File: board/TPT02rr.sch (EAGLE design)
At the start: 16 parts, among them SW4 SW_SLIDECUS12B, U1 MOD_CYBLE014008-00, U2 REG_TPS61221

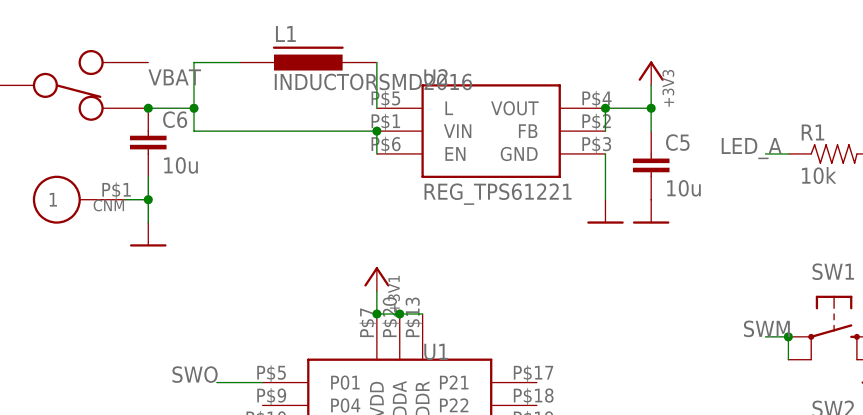
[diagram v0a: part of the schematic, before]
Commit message: Cの部品番号を整理。Elecrow向けBOMを作成。
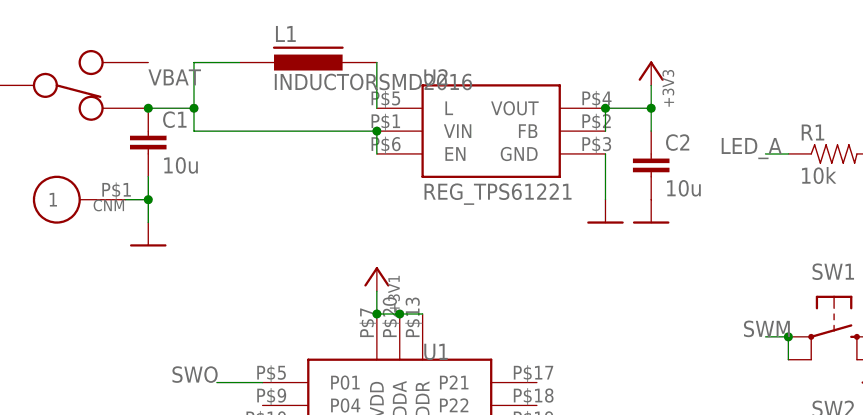
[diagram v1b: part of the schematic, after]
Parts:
- renumbered C5 to C2, C6 to C1
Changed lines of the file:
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@@
 <?xml version="1.0" encoding="utf-8"?>
 <!DOCTYPE eagle SYSTEM "eagle.dtd">
-<eagle version="7.5.0">
+<eagle version="7.7.0">
 <drawing>
 <settings>
@@
 <grid distance="0.1" unitdist="inch" unit="inch" style="lines" multiple="1" display="no" altdistance="0.01" altunitdist="inch" altunit="inch"/>
 <layers>
-<layer number="1" name="Top" color="4" fill="1" visible="yes" active="no"/>
-<layer number="16" name="Bottom" color="1" fill="1" visible="yes" active="no"/>
-<layer number="17" name="Pads" color="2" fill="1" visible="yes" active="no"/>
-<layer number="18" name="Vias" color="2" fill="1" visible="yes" active="no"/>
-<layer number="19" name="Unrouted" color="6" fill="1" visible="yes" active="no"/>
-<layer number="20" name="Dimension" color="15" fill="1" visible="yes" active="no"/>
-<layer number="21" name="tPlace" color="7" fill="1" visible="yes" active="no"/>
-<layer number="22" name="bPlace" color="7" fill="1" visible="yes" active="no"/>
-<layer number="23" name="tOrigins" color="15" fill="1" visible="yes" active="no"/>
-<layer number="24" name="bOrigins" color="15" fill="1" visible="yes" active="no"/>
-<layer number="25" name="tNames" color="7" fill="1" visible="yes" active="no"/>
-<layer number="26" name="bNames" color="7" fill="1" visible="yes" active="no"/>
-<layer number="27" name="tValues" color="7" fill="1" visible="yes" active="no"/>
-<layer number="28" name="bValues" color="7" fill="1" visible="yes" active="no"/>
+<layer number="1" name="Top" color="4" fill="1" visible="no" active="no"/>
+<layer number="16" name="Bottom" color="1" fill="1" visible="no" active="no"/>
+<layer number="17" name="Pads" color="2" fill="1" visible="no" active="no"/>
+<layer number="18" name="Vias" color="2" fill="1" visible="no" active="no"/>
+<layer number="19" name="Unrouted" color="6" fill="1" visible="no" active="no"/>
+<layer number="20" name="Dimension" color="15" fill="1" visible="no" active="no"/>
+<layer number="21" name="tPlace" color="7" fill="1" visible="no" active="no"/>
+<layer number="22" name="bPlace" color="7" fill="1" visible="no" active="no"/>
+<layer number="23" name="tOrigins" color="15" fill="1" visible="no" active="no"/>
+<layer number="24" name="bOrigins" color="15" fill="1" visible="no" active="no"/>
+<layer number="25" name="tNames" color="7" fill="1" visible="no" active="no"/>
+<layer number="26" name="bNames" color="7" fill="1" visible="no" active="no"/>
+<layer number="27" name="tValues" color="7" fill="1" visible="no" active="no"/>
+<layer number="28" name="bValues" color="7" fill="1" visible="no" active="no"/>
 <layer number="29" name="tStop" color="7" fill="3" visible="no" active="no"/>
 <layer number="30" name="bStop" color="7" fill="6" visible="no" active="no"/>
@@
 <layer number="35" name="tGlue" color="7" fill="4" visible="no" active="no"/>
 <layer number="36" name="bGlue" color="7" fill="5" visible="no" active="no"/>
-<layer number="37" name="tTest" color="7" fill="1" visible="yes" active="no"/>
-<layer number="38" name="bTest" color="7" fill="1" visible="yes" active="no"/>
+<layer number="37" name="tTest" color="7" fill="1" visible="no" active="no"/>
+<layer number="38" name="bTest" color="7" fill="1" visible="no" active="no"/>
 <layer number="39" name="tKeepout" color="4" fill="11" visible="no" active="no"/>
 <layer number="40" name="bKeepout" color="1" fill="11" visible="no" active="no"/>
@@
 <layer number="44" name="Drills" color="7" fill="1" visible="no" active="no"/>
 <layer number="45" name="Holes" color="7" fill="1" visible="no" active="no"/>
-<layer number="46" name="Milling" color="3" fill="1" visible="yes" active="no"/>
-<layer number="47" name="Measures" color="7" fill="1" visible="yes" active="no"/>
-<layer number="48" name="Document" color="7" fill="1" visible="yes" active="no"/>
-<layer number="49" name="Reference" color="7" fill="1" visible="yes" active="no"/>
-<layer number="50" name="dxf" color="7" fill="1" visible="yes" active="no"/>
-<layer number="51" name="tDocu" color="7" fill="1" visible="yes" active="no"/>
-<layer number="52" name="bDocu" color="7" fill="1" visible="yes" active="no"/>
-<layer number="53" name="tGND_GNDA" color="7" fill="9" visible="yes" active="no"/>
-<layer number="54" name="bGND_GNDA" color="1" fill="9" visible="yes" active="no"/>
-<layer number="56" name="wert" color="7" fill="1" visible="yes" active="no"/>
-<layer number="57" name="tCAD" color="7" fill="1" visible="yes" active="no"/>
-<layer number="59" name="Invisible" color="7" fill="1" visible="yes" active="no"/>
-<layer number="61" name="stand" color="7" fill="1" visible="yes" active="no"/>
+<layer number="46" name="Milling" color="3" fill="1" visible="no" active="no"/>
+<layer number="47" name="Measures" color="7" fill="1" visible="no" active="no"/>
+<layer number="48" name="Document" color="7" fill="1" visible="no" active="no"/>
+<layer number="49" name="Reference" color="7" fill="1" visible="no" active="no"/>
+<layer number="50" name="dxf" color="7" fill="1" visible="no" active="no"/>
+<layer number="51" name="tDocu" color="7" fill="1" visible="no" active="no"/>
+<layer number="52" name="bDocu" color="7" fill="1" visible="no" active="no"/>
+<layer number="53" name="tGND_GNDA" color="7" fill="9" visible="no" active="no"/>
+<layer number="54" name="bGND_GNDA" color="1" fill="9" visible="no" active="no"/>
+<layer number="56" name="wert" color="7" fill="1" visible="no" active="no"/>
+<layer number="57" name="tCAD" color="7" fill="1" visible="no" active="no"/>
+<layer number="59" name="Invisible" color="7" fill="1" visible="no" active="no"/>
+<layer number="61" name="stand" color="7" fill="1" visible="no" active="no"/>
 <layer number="90" name="Modules" color="5" fill="1" visible="yes" active="yes"/>
 <layer number="91" name="Nets" color="2" fill="1" visible="yes" active="yes"/>
@@
 <part name="+3V3" library="akita" deviceset="POW_+3V3" device=""/>
 <part name="GND3" library="akita" deviceset="POW_GND" device=""/>
-<part name="C5" library="akita" deviceset="CAP" device="0603" value="10u"/>
+<part name="C2" library="akita" deviceset="CAP" device="0603" value="10u"/>
 <part name="GND5" library="akita" deviceset="POW_GND" device=""/>
-<part name="C6" library="akita" deviceset="CAP" device="0603" value="10u"/>
+<part name="C1" library="akita" deviceset="CAP" device="0603" value="10u"/>
 <part name="GND6" library="akita" deviceset="POW_GND" device=""/>
 <part name="CNP" library="akita" deviceset="CON_P01" device="SMD1MM"/>
@@
 <instance part="+3V3" gate="G$1" x="78.74" y="99.06"/>
 <instance part="GND3" gate="1" x="73.66" y="81.28"/>
-<instance part="C5" gate="G$1" x="78.74" y="86.36"/>
+<instance part="C2" gate="G$1" x="78.74" y="86.36"/>
 <instance part="GND5" gate="1" x="78.74" y="81.28"/>
-<instance part="C6" gate="G$1" x="22.86" y="88.9"/>
+<instance part="C1" gate="G$1" x="22.86" y="88.9"/>
 <instance part="GND6" gate="1" x="22.86" y="78.74"/>
 <instance part="CNP" gate="G$1" x="-2.54" y="96.52" rot="R180"/>
@@
 </segment>
 <segment>
-<pinref part="C5" gate="G$1" pin="2"/>
+<pinref part="C2" gate="G$1" pin="2"/>
 <pinref part="GND5" gate="1" pin="GND"/>
 </segment>
 <segment>
-<pinref part="C6" gate="G$1" pin="2"/>
+<pinref part="C1" gate="G$1" pin="2"/>
 <pinref part="GND6" gate="1" pin="GND"/>
 <wire x1="22.86" y1="86.36" x2="22.86" y2="83.82" width="0.1524" layer="91"/>
@@
 <wire x1="73.66" y1="93.98" x2="78.74" y2="93.98" width="0.1524" layer="91"/>
 <wire x1="78.74" y1="93.98" x2="78.74" y2="96.52" width="0.1524" layer="91"/>
-<pinref part="C5" gate="G$1" pin="1"/>
+<pinref part="C2" gate="G$1" pin="1"/>
 <wire x1="78.74" y1="93.98" x2="78.74" y2="91.44" width="0.1524" layer="91"/>
 <junction x="78.74" y="93.98"/>
@@
 <net name="VBAT" class="0">
 <segment>
-<pinref part="C6" gate="G$1" pin="1"/>
+<pinref part="C1" gate="G$1" pin="1"/>
 <pinref part="SW4" gate="G$1" pin="P$1"/>
 <label x="22.86" y="96.52" size="1.778" layer="95"/>
